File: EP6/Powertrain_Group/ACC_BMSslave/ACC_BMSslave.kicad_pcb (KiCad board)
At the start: 4 copper layers, 100 x 50 mm, 268 parts, among them IC1 ADBMS1818ASWAZ-R7, IC10 NX2301P,215, IC11 NX2301P,215, IC12 NX2301P,215, IC13 NX2301P,215, IC14 NX2301P,215, IC15 NX2301P,215, IC16 NX2301P,215, IC17 NX2301P,215, IC2 LT8631IFE#PBF, IC3 NX2301P,215, IC4 NX2301P,215, IC5 NX2301P,215, IC6 NX2301P,215, IC7 NX2301P,215, IC8 NX2301P,215, IC9 NX2301P,215, J1 Cell taps, J2 Temp probes A, J3 Temp probes B, J4 Temp probes C, J5 Temp probes D, J6 RJ45, J7 RJ45, J8 isoSPI_out, J9 isoSPI_in, U1 LM324DT, U2 ADG758CPZ, U3 ADG758CPZ, U4 ADG758CPZ, U5 ADG758CPZ

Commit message: ACC_BMSslave pcb priliminary layout
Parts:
- C1, C10, C11, C12, C13, C2, C23, C24, C25, C26, C3, C4, C7, C8, C9: footprint Capacitor_SMD:C_0201_0603Metric -> Capacitor_SMD:C_0603_1608Metric
- C27, C29, C31, C33, C35, C37, C39, C41, C43, C45, C47, C49, C51, C53, C55: footprint Capacitor_SMD:C_0603_1608Metric -> Capacitor_SMD:C_0805_2012Metric
- C28, C30, C32, C34, C36, C38, C40, C42, C44, C46, C48, C50, C52, C54, C56: footprint Capacitor_SMD:C_0603_1608Metric -> Capacitor_SMD:C_0402_1005Metric
- D1, D10, D11, D12, D13, D14, D15, D16, D17, D2, D3, D4, D5, D6, D7, D8, D9: footprint LED_SMD:LED_0805_2012Metric -> LED_SMD:LED_0603_1608Metric
- R1, R10, R102, R11, R12, R123, R124, R125, R126, R127, R13, R14, R15, R16, R17, R18, R19, R2, R20, R21, R22, R23, R24, R25, R26, R27, R28, R29, R3, R30, R31, R32, R33, R34, R35, R36, R37, R38, R4, R5, R50, R51, R52, R6, R61, R66, R7, R71, R76, R8, R81, R86, R9, R91, R96, R97: footprint Resistor_SMD:R_0603_1608Metric -> Resistor_SMD:R_0402_1005Metric
- U1: footprint Package_SO:SOIC-14-16_3.9x9.9mm_P1.27mm -> Package_SO:SO-14_3.9x8.65mm_P1.27mm
- moved C23 199.1 mm to (60.0, 68.8), turned to -90 degrees
- moved U2 197.7 mm to (63.5, 67.0), turned to 180 degrees
- moved C24 190.1 mm to (69.2, 68.8), turned to -90 degrees
- moved U3 188.2 mm to (72.8, 67.0), turned to 180 degrees
- moved C25 163.2 mm to (95.0, 68.8), turned to -90 degrees
- moved D1 162.4 mm to (58.5, 127.0)
- moved U4 161.7 mm to (98.5, 67.0), turned to 180 degrees
- moved C1 161.6 mm to (45.8, 57.8)
- moved C2 161.6 mm to (45.8, 59.5)
- moved C3 161.6 mm to (45.8, 61.2)
- moved C4 161.6 mm to (45.8, 63.0)
- moved R16 160.3 mm to (53.5, 62.0)
- moved R33 158.1 mm to (74.8, 121.8), turned to 90 degrees
- moved R15 156.2 mm to (57.5, 62.0)
- moved R8 154.4 mm to (55.5, 62.0), turned to 180 degrees
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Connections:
- D10 pad 1: Net-(D10-K) -> /CT7
- D11 pad 1: Net-(D11-K) -> /CT8
- D12 pad 1: Net-(D12-K) -> /CT9
- D13 pad 1: Net-(D13-K) -> /CT10
- D14 pad 1: Net-(D14-K) -> /CT11
- D15 pad 1: Net-(D15-K) -> /CT12
- D16 pad 1: Net-(D16-K) -> /CT13
- D17 pad 1: Net-(D17-K) -> /CT14
- D3 pad 1: Net-(D3-K) -> /CT1
- D4 pad 1: Net-(D4-K) -> Earth
- D5 pad 1: Net-(D5-K) -> /CT2
- D6 pad 1: Net-(D6-K) -> /CT3
- D7 pad 1: Net-(D7-K) -> /CT4
- D8 pad 1: Net-(D8-K) -> /CT5
- D9 pad 1: Net-(D9-K) -> /CT6
- IC10 pad 3: Net-(D10-A) -> Net-(IC10-D)
- IC11 pad 3: Net-(D11-A) -> Net-(IC11-D)
- IC12 pad 3: Net-(D12-A) -> Net-(IC12-D)
- IC13 pad 3: Net-(D13-A) -> Net-(IC13-D)
- IC14 pad 3: Net-(D14-A) -> Net-(IC14-D)
- IC15 pad 3: Net-(D15-A) -> Net-(IC15-D)
- IC16 pad 3: Net-(D16-A) -> Net-(IC16-D)
- IC17 pad 3: Net-(D17-A) -> Net-(IC17-D)
- IC3 pad 3: Net-(D3-A) -> Net-(IC3-D)
- IC4 pad 3: Net-(D4-A) -> Net-(IC4-D)
- IC5 pad 3: Net-(D5-A) -> Net-(IC5-D)
- IC6 pad 3: Net-(D6-A) -> Net-(IC6-D)
- IC7 pad 3: Net-(D7-A) -> Net-(IC7-D)
- IC8 pad 3: Net-(D8-A) -> Net-(IC8-D)
- IC9 pad 3: Net-(D9-A) -> Net-(IC9-D)
- R100 pad 2: Net-(D12-A) -> Net-(IC12-D)
- R103 pad 1: Net-(D13-K) -> Net-(IC13-D)
- R103 pad 2: /CT10 -> Net-(D13-A)
- R104 pad 2: Net-(D13-A) -> Net-(IC13-D)
- R105 pad 2: Net-(D13-A) -> Net-(IC13-D)
- R107 pad 1: Net-(D14-K) -> Net-(IC14-D)
- R107 pad 2: /CT11 -> Net-(D14-A)
- R108 pad 2: Net-(D14-A) -> Net-(IC14-D)
- R109 pad 2: Net-(D14-A) -> Net-(IC14-D)
- R111 pad 1: Net-(D15-K) -> Net-(IC15-D)
- R111 pad 2: /CT12 -> Net-(D15-A)
- R112 pad 2: Net-(D15-A) -> Net-(IC15-D)
- R113 pad 2: Net-(D15-A) -> Net-(IC15-D)
- R115 pad 1: Net-(D16-K) -> Net-(IC16-D)
- R115 pad 2: /CT13 -> Net-(D16-A)
- R116 pad 2: Net-(D16-A) -> Net-(IC16-D)
- R117 pad 2: Net-(D16-A) -> Net-(IC16-D)
- R119 pad 1: Net-(D17-K) -> Net-(IC17-D)
- R119 pad 2: /CT14 -> Net-(D17-A)
- R120 pad 2: Net-(D17-A) -> Net-(IC17-D)
- R121 pad 2: Net-(D17-A) -> Net-(IC17-D)
- R53 pad 1: Net-(D3-K) -> Net-(IC3-D)
- R53 pad 2: /CT1 -> Net-(D3-A)
- R54 pad 2: Net-(D3-A) -> Net-(IC3-D)
- R55 pad 2: Net-(D3-A) -> Net-(IC3-D)
- R57 pad 1: Net-(D4-K) -> Net-(IC4-D)
- R57 pad 2: Earth -> Net-(D4-A)
- R58 pad 2: Net-(D4-A) -> Net-(IC4-D)
- R59 pad 2: Net-(D4-A) -> Net-(IC4-D)
- R62 pad 1: Net-(D5-K) -> Net-(IC5-D)
- R62 pad 2: /CT2 -> Net-(D5-A)
- R63 pad 2: Net-(D5-A) -> Net-(IC5-D)
- R64 pad 2: Net-(D5-A) -> Net-(IC5-D)
- R67 pad 1: Net-(D6-K) -> Net-(IC6-D)
- R67 pad 2: /CT3 -> Net-(D6-A)
- R68 pad 2: Net-(D6-A) -> Net-(IC6-D)
- R69 pad 2: Net-(D6-A) -> Net-(IC6-D)
- R72 pad 1: Net-(D7-K) -> Net-(IC7-D)
- R72 pad 2: /CT4 -> Net-(D7-A)
- R73 pad 2: Net-(D7-A) -> Net-(IC7-D)
- R74 pad 2: Net-(D7-A) -> Net-(IC7-D)
- R77 pad 1: Net-(D8-K) -> Net-(IC8-D)
- R77 pad 2: /CT5 -> Net-(D8-A)
- R78 pad 2: Net-(D8-A) -> Net-(IC8-D)
- R79 pad 2: Net-(D8-A) -> Net-(IC8-D)
- R82 pad 1: Net-(D9-K) -> Net-(IC9-D)
- R82 pad 2: /CT6 -> Net-(D9-A)
- R83 pad 2: Net-(D9-A) -> Net-(IC9-D)
- R84 pad 2: Net-(D9-A) -> Net-(IC9-D)
- R87 pad 1: Net-(D10-K) -> Net-(IC10-D)
- R87 pad 2: /CT7 -> Net-(D10-A)
- R88 pad 2: Net-(D10-A) -> Net-(IC10-D)
- R89 pad 2: Net-(D10-A) -> Net-(IC10-D)
- R92 pad 1: Net-(D11-K) -> Net-(IC11-D)
- R92 pad 2: /CT8 -> Net-(D11-A)
- R93 pad 2: Net-(D11-A) -> Net-(IC11-D)
- R94 pad 2: Net-(D11-A) -> Net-(IC11-D)
- R98 pad 1: Net-(D12-K) -> Net-(IC12-D)
- R98 pad 2: /CT9 -> Net-(D12-A)
- R99 pad 2: Net-(D12-A) -> Net-(IC12-D)
- U2 pad 10: /T0 -> /T6
- U2 pad 11: /T1 -> /T14
- U2 pad 12: /T2 -> /T7
- U2 pad 13: /T3 -> /T15
- U2 pad 4: /T5 -> /T12
- U2 pad 5: /T6 -> /T5
- U2 pad 6: /T7 -> /T13
- U3 pad 10: /T8 -> /T2
- U3 pad 11: /T9 -> /T10
- U3 pad 12: /T10 -> /T3
- U3 pad 3: /T12 -> /T0
- U3 pad 4: /T13 -> /T8
- U3 pad 5: /T14 -> /T1
- U3 pad 6: /T15 -> /T9
- U4 pad 10: /T16 -> /T22
- U4 pad 11: /T17 -> /T30
- U4 pad 12: /T18 -> /T23
- U4 pad 13: /T19 -> /T31
- U4 pad 4: /T21 -> /T28
- U4 pad 5: /T22 -> /T21
- U4 pad 6: /T23 -> /T29
- U5 pad 10: /T24 -> /T18
- U5 pad 11: /T25 -> /T26
- U5 pad 12: /T26 -> /T19
- U5 pad 3: /T28 -> /T16
- U5 pad 4: /T29 -> /T24
- U5 pad 5: /T30 -> /T17
- U5 pad 6: /T31 -> /T25
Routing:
- net /CT15: track 0.00 -> 75.3 mm, vias 0 -> 3
- net /CT10: track 0.00 -> 60.0 mm, vias 0 -> 5
- net /CT13: track 0.00 -> 56.1 mm, vias 0 -> 4
- net /CT5: track 0.00 -> 54.8 mm, vias 0 -> 5
- net /CT14: track 0.00 -> 54.3 mm, vias 0 -> 5
- net /CT12: track 0.00 -> 54.1 mm, vias 0 -> 5
- net /CT11: track 0.00 -> 50.4 mm, vias 0 -> 4
- net /CT9: track 0.00 -> 50.2 mm, vias 0 -> 4
- net /CT7: track 0.00 -> 49.8 mm, vias 0 -> 4
- net /CT8: track 0.00 -> 47.7 mm, vias 0 -> 4
- net /CT6: track 0.00 -> 47.4 mm, vias 0 -> 4
- net /S15: track 0.00 -> 47.3 mm, vias 0 -> 2
- net /CT4: track 0.00 -> 46.6 mm, vias 0 -> 4
- net /S1: track 0.00 -> 46.0 mm, vias 0 -> 2
- net /CT3: track 0.00 -> 45.9 mm, vias 0 -> 4
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- added copper zone on In1.Cu, net Earth
- added copper zone on In2.Cu, net Earth
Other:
- board size 100 x 50 mm -> 100 x 80 mm

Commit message: ACC_BMSslave pcb layout kinda done
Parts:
- added ?: , Graphics, F.Cu at (70.0, 74.5)
- added ? (x4): , Graphics, F.Cu at (70.5, 77.2)
- added ?: , Graphics, B.Cu at (70.5, 77.2)
- added J10: Cell taps B, Connector_JST:JST_XH_B8B-XH-A_1x08_P2.50mm_Vertical, F.Cu at (147.0, 100.2)
- C10, C11, C14, C15, C8, C9: footprint Capacitor_SMD:C_0603_1608Metric -> Capacitor_SMD:C_0402_1005Metric
- J1: value Cell taps -> Cell taps A; footprint Connector_JST:JST_XH_B16B-XH-A_1x16_P2.50mm_Vertical -> Connector_JST:JST_XH_B8B-XH-A_1x08_P2.50mm_Vertical
- R33: footprint Resistor_SMD:R_0402_1005Metric -> Resistor_SMD:R_0805_2012Metric
- R34: footprint Resistor_SMD:R_0402_1005Metric -> Resistor_SMD:R_0603_1608Metric
- R39, R46, R47: footprint Resistor_SMD:R_0201_0603Metric -> Resistor_SMD:R_0603_1608Metric
- R40, R41, R42, R43, R44, R45, R48, R49: footprint Resistor_SMD:R_0201_0603Metric -> Resistor_SMD:R_0402_1005Metric
- moved C2 72.8 mm to (118.4, 64.4), turned to 180 degrees
- moved C1 57.9 mm to (103.2, 65.2), turned to -90 degrees
- moved C4 40.2 mm to (86.0, 62.6)
- moved D1 37.1 mm to (90.2, 107.8), turned to -90 degrees
- moved R39 35.7 mm to (92.5, 110.5)
- moved R33 28.4 mm to (103.0, 124.8), turned to 180 degrees
- moved C5 28.3 mm to (103.0, 126.6), turned to 0 degrees
- moved C3 22.8 mm to (68.2, 65.2), turned to -90 degrees
- moved R41 17.3 mm to (80.6, 67.8)
- moved R40 15.8 mm to (80.6, 70.8)
- moved C8 15.4 mm to (79.6, 70.8), turned to 90 degrees
- moved C9 15.3 mm to (79.6, 67.8), turned to 90 degrees
- moved D2 13.4 mm to (90.2, 104.2), turned to -90 degrees
- moved R42 13.0 mm to (91.0, 67.8)
- moved C6 10.6 mm to (91.8, 100.4)
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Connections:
- C10 pad 1: /GPIO8 -> /GPIO6
- C11 pad 1: /GPIO9 -> /GPIO7
- C8 pad 1: /GPIO6 -> /GPIO8
- C9 pad 1: /GPIO7 -> /GPIO9
- D1 pad 1: Net-(D1-K) -> Earth
- D1 pad 2: VREG -> Net-(D1-A)
- F10 pad 1: Net-(J1-Pin_10) -> Net-(J10-Pin_2)
- F11 pad 1: Net-(J1-Pin_11) -> Net-(J10-Pin_3)
- F12 pad 1: Net-(J1-Pin_12) -> Net-(J10-Pin_4)
- F13 pad 1: Net-(J1-Pin_13) -> Net-(J10-Pin_5)
- F14 pad 1: Net-(J1-Pin_14) -> Net-(J10-Pin_6)
- F15 pad 1: Net-(J1-Pin_15) -> Net-(J10-Pin_7)
- F16 pad 1: Net-(J1-Pin_16) -> Net-(J10-Pin_8)
- F9 pad 1: Net-(J1-Pin_9) -> Net-(J10-Pin_1)
- R39 pad 1: Net-(D1-K) -> Net-(D1-A)
- R39 pad 2: Earth -> VREG
- R40 pad 2: /GPIO6 -> /GPIO8
- R41 pad 1: Net-(U1B--) -> Net-(U1D--)
- R41 pad 2: /GPIO7 -> /GPIO9
- R42 pad 2: /GPIO8 -> /GPIO6
- R43 pad 1: Net-(U1D--) -> Net-(U1B--)
- R43 pad 2: /GPIO9 -> /GPIO7
- U1 pad 12: /tprobe_mux4/OUT -> /tprobe_mux2/OUT
- U1 pad 5: /tprobe_mux2/OUT -> /tprobe_mux4/OUT
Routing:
- net VREG: track 0.00 -> 190.1 mm, vias 0 -> 12
- net /VREF2: track 30.6 -> 143.2 mm, vias 16 -> 21
- net Earth: track 24.7 -> 111.6 mm, vias 19 -> 79
- net /GPIO2: track 0.00 -> 69.2 mm, vias 0 -> 4
- net /GPIO3: track 0.00 -> 67.4 mm, vias 0 -> 4
- net /GPIO1: track 0.00 -> 65.7 mm, vias 0 -> 4
- net /power/VIN: track 0.00 -> 50.9 mm
- net /DRIVE: track 0.00 -> 50.9 mm, vias 0 -> 2
- net /GPIO9: track 0.00 -> 28.6 mm
- net /GPIO8: track 0.00 -> 24.6 mm
- net /tprobe_mux4/OUT: track 1.34 -> 25.7 mm, vias 1 -> 2
- net /tprobe_mux1/OUT: track 1.27 -> 25.4 mm, vias 1 -> 2
- net /IN_P: track 0.00 -> 23.3 mm
- net /IN_N: track 0.00 -> 23.2 mm
- net Net-(J9-Pin_2): track 0.00 -> 21.2 mm
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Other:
- board size 100 x 80 mm -> 100 x 79 mm
- board text added: "+"
- board text added: "+ -"
- board text added: "-"
- board text added: "..."
- board text added: "5V OK"
- board text added: "75.6V 18S"
- board text added: "ACC_BMSslave"
- board text added: "EP6"
- board text added: "T0"
- board text added: "T14"
- board text added: "T15"
- board text added: "T16"
- board text added: "T23"
- board text added: "T24"
- board text added: "T32"
- board text added: "T6"
- board text added: "T7"
- board text added: "T8"
- board text added: "Watchdog"
- board text added: "isoSPI IN"
- board text added: "isoSPI OUT"
- board text added: "version 1.0 2025/01/15 jerrymk"

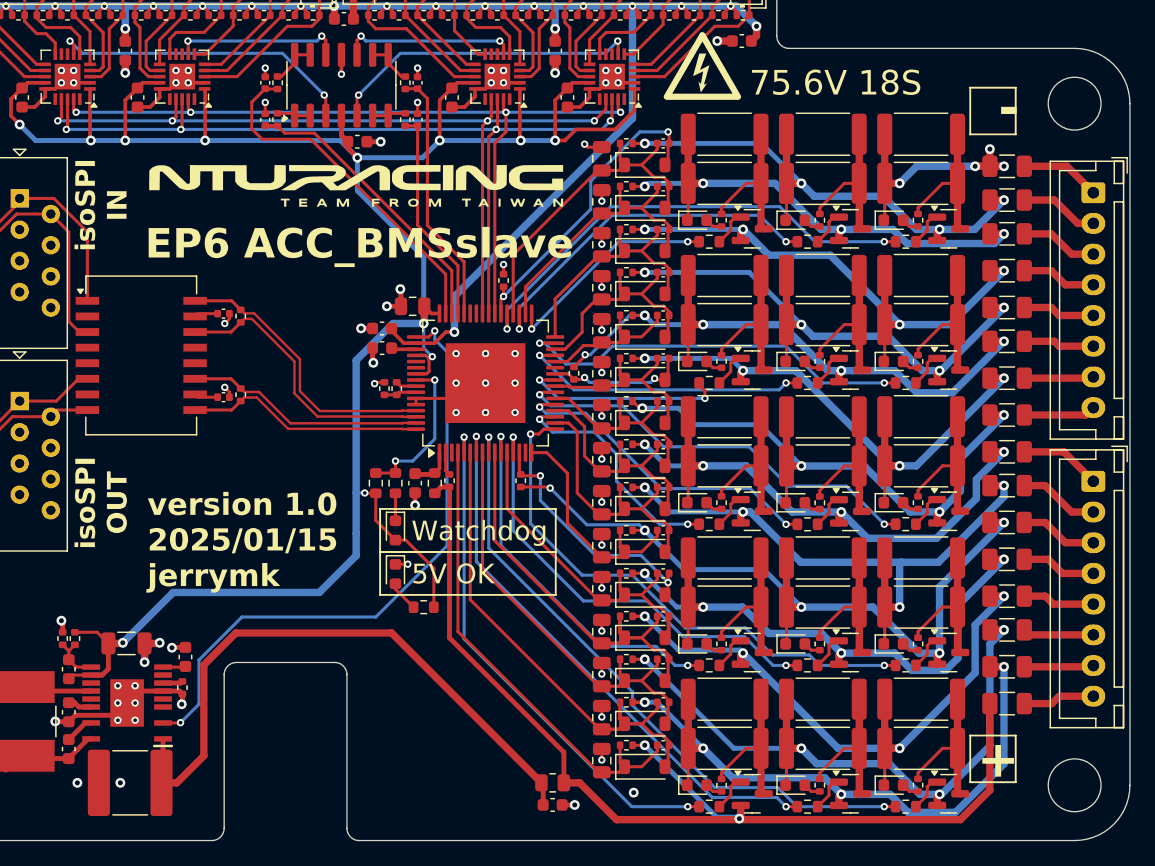
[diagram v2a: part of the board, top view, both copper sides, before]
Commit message: ACC_BMSslave fix routing issue (split input connector)
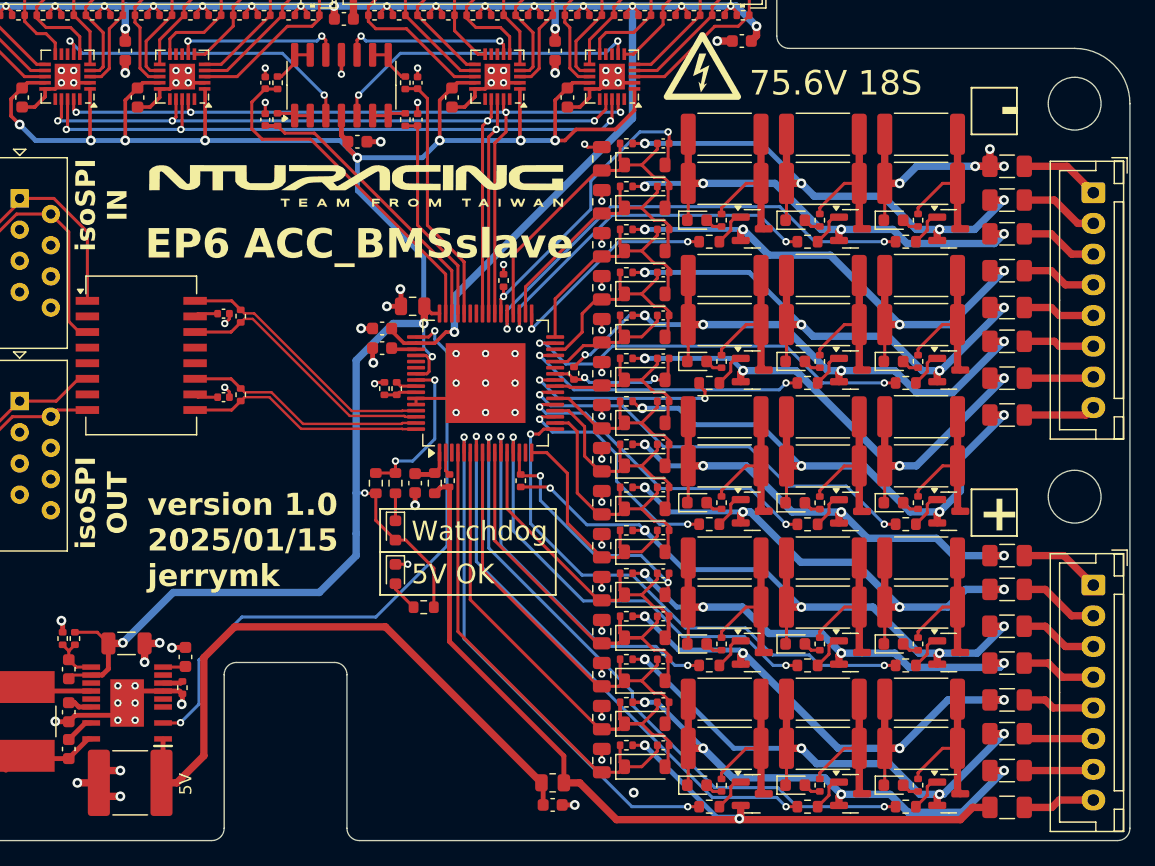
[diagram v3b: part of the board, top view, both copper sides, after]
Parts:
- moved H4 23.5 mm to (145.5, 101.5)
- moved F10 8.45 mm to (140.0, 109.0)
- moved F11 8.45 mm to (140.0, 112.0)
- moved F12 8.45 mm to (140.0, 115.0)
- moved F13 8.45 mm to (140.0, 118.0)
- moved F14 8.45 mm to (140.0, 120.8)
- moved F15 8.45 mm to (140.0, 123.8)
- moved F16 8.45 mm to (140.0, 126.8)
- moved F9 8.45 mm to (140.0, 106.3)
- moved J10 8.45 mm to (147.0, 108.7)
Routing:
- net /CT13: track 55.6 -> 47.2 mm
- net /CT14: track 54.8 -> 46.7 mm
- net /CT15: track 85.6 -> 78.0 mm
- net Earth: track 111.6 -> 118.7 mm, vias 79 -> 80
- net /CT10: track 63.9 -> 57.2 mm
- net /CT11: track 50.2 -> 44.0 mm
- net /CT12: track 53.5 -> 47.7 mm
- net /CT9: track 50.0 -> 45.2 mm
- net /CT8: track 47.6 -> 44.4 mm
- net /IN_N: track 23.2 -> 21.7 mm
- net /IN_P: track 23.3 -> 21.7 mm
- net /power/VIN: track 50.9 -> 51.6 mm
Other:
- outline, holes or cut-outs redrawn
- board text added: "5V"

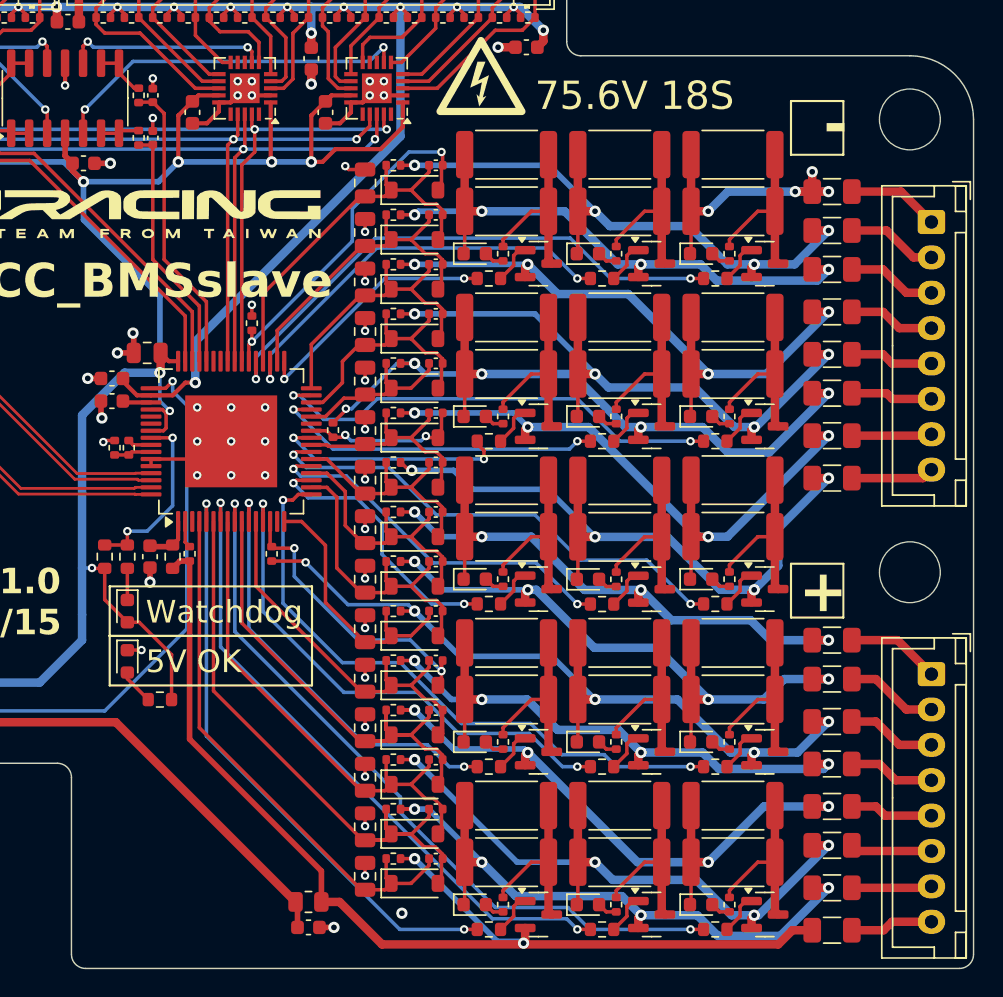
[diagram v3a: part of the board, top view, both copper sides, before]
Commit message: ACC_BMSslave fix routing issue (joint input connector)
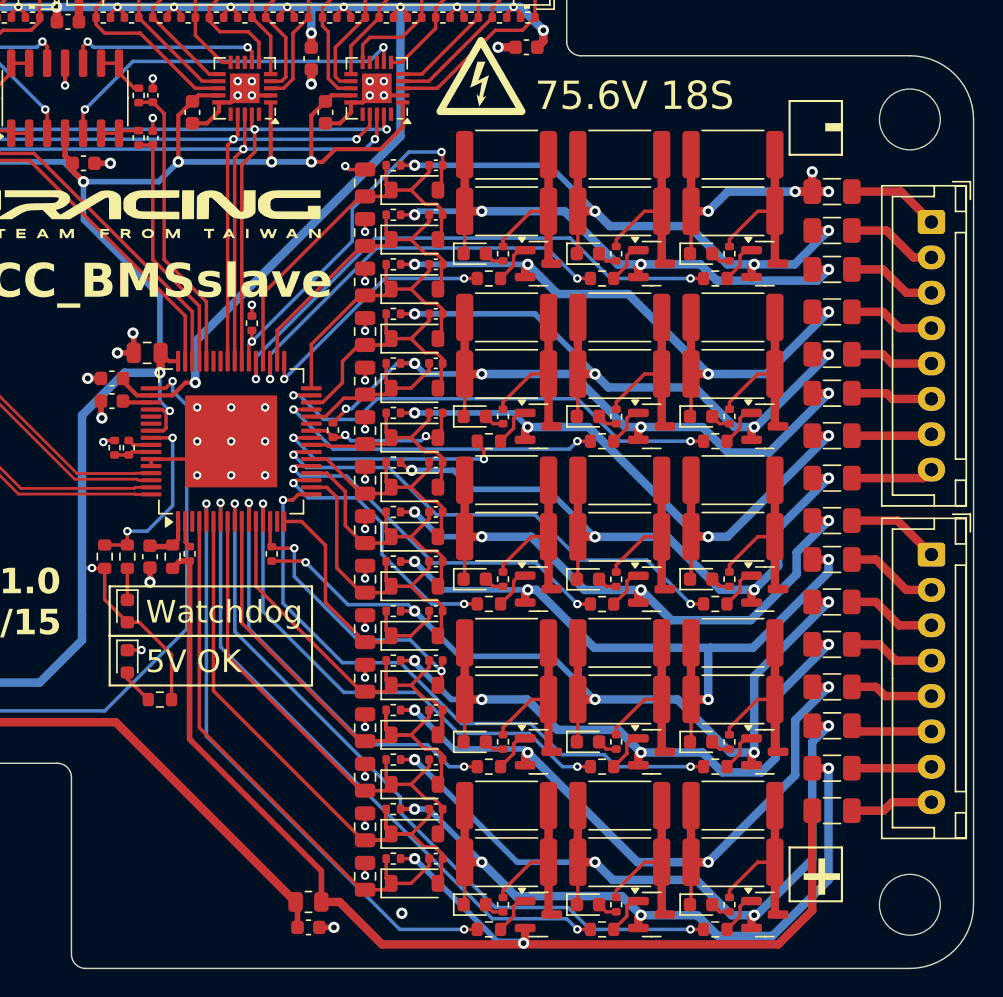
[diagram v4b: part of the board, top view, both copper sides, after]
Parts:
- moved H4 23.5 mm to (145.5, 125.0)
- moved F10 8.45 mm to (140.0, 100.6)
- moved F11 8.45 mm to (140.0, 103.6)
- moved F12 8.45 mm to (140.0, 106.6)
- moved F13 8.45 mm to (140.0, 109.6)
- moved F14 8.45 mm to (140.0, 112.3)
- moved F15 8.45 mm to (140.0, 115.3)
- moved F16 8.45 mm to (140.0, 118.3)
- moved F9 8.45 mm to (140.0, 97.8)
- moved J10 8.45 mm to (147.0, 100.2)
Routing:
- net /CT13: track 47.2 -> 55.6 mm
- net /CT14: track 46.7 -> 54.8 mm
- net /CT15: track 78.0 -> 85.6 mm
- net /CT10: track 57.2 -> 63.9 mm
- net /CT11: track 44.0 -> 50.2 mm
- net /CT12: track 47.7 -> 53.5 mm
- net /CT9: track 45.2 -> 50.0 mm
- net /CT8: track 44.4 -> 47.6 mm
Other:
- outline, holes or cut-outs redrawn

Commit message: ACC_BMSslave fix silk
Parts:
- moved ? 0.30 mm to (69.7, 74.5)
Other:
- board text added: "63V 15S"
- board text added: "A(in)"
- board text added: "B(out)"
- board text removed: "75.6V 18S"
- board text removed: "isoSPI IN"
- board text removed: "isoSPI OUT"
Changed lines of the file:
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@@
 	(footprint "Graphics"
 		(layer "F.Cu")
-		(at 70 74.5)
+		(at 69.6985 74.5)
 		(property "Reference" ""
 			(at 0 0 0)
@@
 	)
 	(gr_text "ACC_BMSslave"
-		(at 77.853 82.3225 0)
+		(at 77.5515 82.3225 0)
 		(layer "F.SilkS")
 		(effects
@@
 		)
 	)
-	(gr_text "75.6V 18S"
+	(gr_text "63V 15S"
 		(at 119 69 0)
 		(layer "F.SilkS")
@@
 		)
 	)
-	(gr_text "isoSPI\nOUT"
-		(at 68.5 102 90)
+	(gr_text "B(out)"
+		(at 66.1 100.5 90)
 		(layer "F.SilkS" knockout)
 		(effects
@@
 		)
 	)
-	(gr_text "isoSPI\nIN"
-		(at 68.5 77.75 90)
+	(gr_text "A(in)"
+		(at 66 80 90)
 		(layer "F.SilkS" knockout)
 		(effects
@@
 	)
 	(gr_text "EP6"
-		(at 69.8015 82.3225 0)
+		(at 69.5 82.3225 0)
 		(layer "F.SilkS" knockout)
 		(effects
